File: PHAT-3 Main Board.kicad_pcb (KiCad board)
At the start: 2 copper layers, 18 parts, among them P1 Power Terminal Block, P2 Power Terminal Block, P3 Power Terminal Block, P4 Power Terminal Block, Q1 IRLZ44N, U1 AHT21, U10 Logic Level Converter, U2 ESP32-S3 Dual-core SX1262, U3 BME280, U4 GY-521 MPU-6050, U5 LM2596, U6 GT-7U, U7 SCD41, U8 uCAM-III, U9 SD Card Reader

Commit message: Rewired Everything Again
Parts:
- added R4: 100, Resistor_THT:R_Axial_DIN0207_L6.3mm_D2.5mm_P10.16mm_Horizontal, F.Cu at (104.1, 142.8)
- added R5: 10k, Resistor_THT:R_Axial_DIN0207_L6.3mm_D2.5mm_P10.16mm_Horizontal, F.Cu at (104.1, 146.8)
- added R6: 10k, Resistor_THT:R_Axial_DIN0207_L6.3mm_D2.5mm_P10.16mm_Horizontal, F.Cu at (104.1, 150.9)
- added R7: 10k, Resistor_THT:R_Axial_DIN0207_L6.3mm_D2.5mm_P10.16mm_Horizontal, F.Cu at (104.1, 154.9)
- U3: value BME280 -> GY-68 BMP180; footprint Actual Footprint Library:BME280 -> Actual Footprint Library:GY-68 BMP180
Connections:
- R1 pad 2: Net-(U1-SDA) -> Net-(U10-HV1)
- R2 pad 1: Net-(U1-SCL) -> Net-(U10-HV2)
- U1 pad 1: +5V -> +3V3
- U10 pad 1: Net-(U10-LV1) -> Net-(U1-SCL)
- U10 pad 11: Net-(U1-SCL) -> Net-(U10-HV2)
- U10 pad 12: Net-(U1-SDA) -> Net-(U10-HV1)
- U10 pad 2: Net-(U10-LV2) -> Net-(U1-SDA)
- U10 pad 3: Net-(U10-LV) -> +3V3
- U2 pad 13: Net-(U10-LV2) -> Net-(U1-SCL)
- U2 pad 14: Net-(U10-LV1) -> Net-(U1-SDA)
- U2 pad 16: Net-(U10-LV) -> unconnected-(U2-3V3-Pad16)
- U2 pad 17: unconnected-(U2-3V3-Pad17) -> +3V3
- U2 pad 18: unconnected-(U2-GND-Pad18) -> GND
- U2 pad 28: Net-(Q1-G) -> Net-(U2-HTR)
- U3 pad 1: +5V -> +3V3
- U4 pad 3: Net-(U1-SCL) -> Net-(U10-HV1)
- U4 pad 4: Net-(U1-SDA) -> Net-(U10-HV2)
- U7 pad 1: unconnected-(U7-GND-Pad1) -> GND
- U7 pad 2: +5V -> +3V3

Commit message: Updated Footprint Sizes and SD Card Reader
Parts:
- added C1: 100uF, Capacitor_THT:C_Radial_D5.0mm_H11.0mm_P2.00mm, F.Cu at (155.5, 154.9)
- added C2: 100nF, Capacitor_THT:C_Disc_D3.0mm_W2.0mm_P2.50mm, F.Cu at (149.1, 153.4)
- added C3: 100nF, Capacitor_THT:C_Disc_D3.0mm_W2.0mm_P2.50mm, F.Cu at (149.1, 157.0)
- added REF**: MountingHole_3.2mm_M3, MountingHole:MountingHole_3.2mm_M3, F.Cu at (187.3, 128.3)
- added REF**: MountingHole_3.2mm_M3, MountingHole:MountingHole_3.2mm_M3, F.Cu at (101.6, 50.8)
- added REF**: MountingHole_3.2mm_M3, MountingHole:MountingHole_3.2mm_M3, F.Cu at (187.3, 54.6)
- added REF**: MountingHole_3.2mm_M3, MountingHole:MountingHole_3.2mm_M3, F.Cu at (101.6, 130.8)
- U9: value SD Card Reader -> SDHC; footprint Actual Footprint Library:SD Card Reader -> Actual Footprint Library:SDHC
- moved P1 112.1 mm to (218.4, 114.3)
- moved R1 108.4 mm to (266.7, 77.2)
- moved R2 108.4 mm to (266.7, 81.3)
- moved U3 105.6 mm to (266.2, 52.1)
- moved U5 105.3 mm to (23.2, 120.5)
- moved U4 103.7 mm to (63.5, 132.1)
- moved U10 93.3 mm to (250.2, 141.0)
- moved P2 77.2 mm to (131.5, 162.9)
- moved P3 77.2 mm to (131.5, 174.8)
- moved P4 77.2 mm to (131.5, 186.7)
- moved U9 70.2 mm to (226.3, 45.8)
- moved U2 62.7 mm to (143.5, 69.8)
- moved U6 53.2 mm to (121.9, 73.7), turned to 180 degrees
- moved R3 49.4 mm to (207.0, 81.3)
- moved Q1 48.9 mm to (65.7, 167.6)
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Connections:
- U2 pad 29: Net-(U2-CS) -> Net-(U2-MISO)
- U2 pad 30: Net-(U2-SCK) -> Net-(U2-CLK)
- U2 pad 32: Net-(U2-MISO) -> Net-(U2-CS)
- U9 pad 1: Net-(U2-CS) -> +3V3
- U9 pad 2: Net-(U2-SCK) -> Net-(U2-CS)
- U9 pad 4: Net-(U2-MISO) -> Net-(U2-CLK)
- U9 pad 5: +5V -> Net-(U2-MISO)
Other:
- board outline added: 95.9 x 90.2 mm
- copper layers 2 -> 6

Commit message: Made a Preliminary PCB Layout
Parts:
- added C4: 100uF, Capacitor_THT:C_Radial_D5.0mm_H11.0mm_P2.00mm, F.Cu at (188.6, 63.5)
- U1, U3, U7: moved to B.Cu
- moved U5 162.7 mm to (169.5, 49.5), turned to 180 degrees
- moved R2 138.0 mm to (136.5, 127.0)
- moved R1 137.8 mm to (136.5, 122.6)
- moved U10 135.0 mm to (116.9, 119.4)
- moved R4 134.9 mm to (176.5, 95.2), turned to 180 degrees
- moved R5 132.6 mm to (166.4, 90.8)
- moved U4 123.5 mm to (186.7, 123.2), turned to 180 degrees
- moved Q1 122.5 mm to (168.9, 101.6)
- moved C1 110.5 mm to (118.7, 50.8)
- moved U3 104.6 mm to (178.9, 109.9), turned to 180 degrees
- moved U1 98.3 mm to (141.6, 111.1), turned to -90 degrees
- moved P3 94.2 mm to (184.8, 97.2), turned to 90 degrees
- moved U7 93.7 mm to (119.4, 77.6), turned to 90 degrees
- moved R6 73.1 mm to (99.7, 118.7)
- moved R7 72.1 mm to (99.7, 123.8)
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
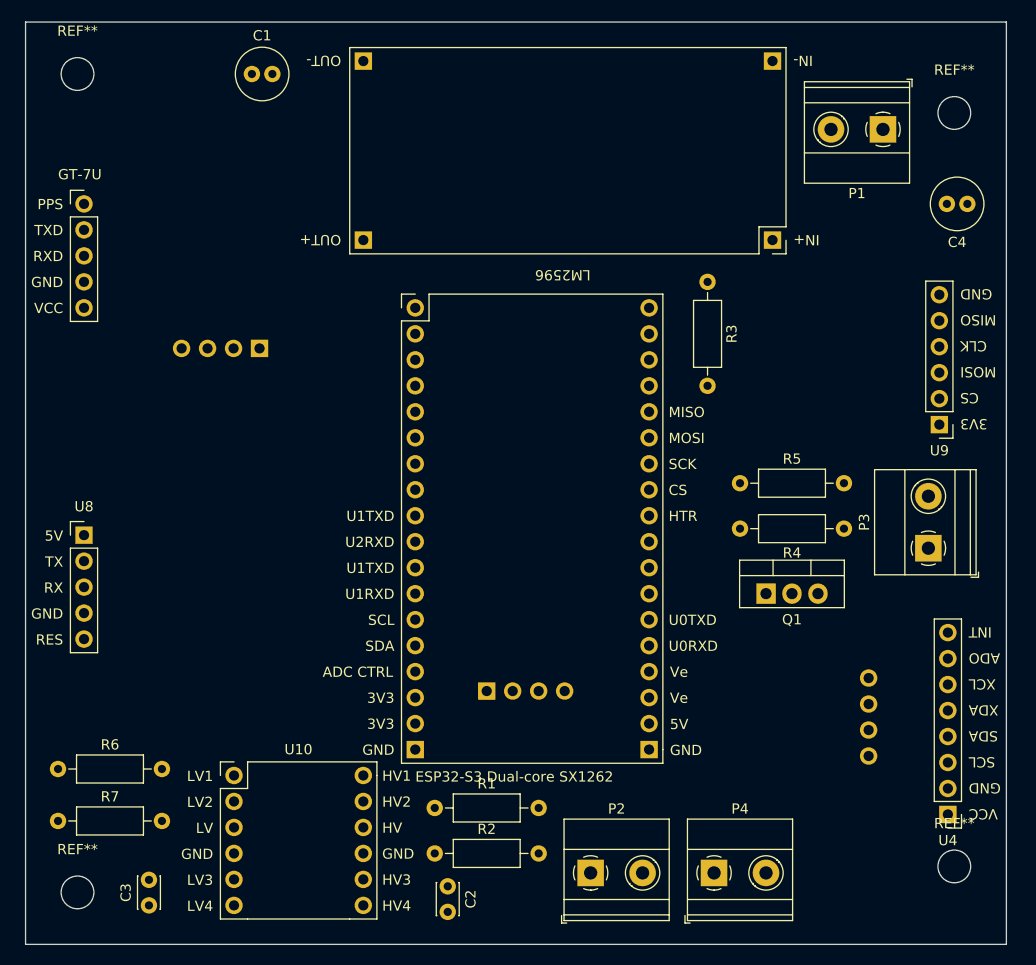
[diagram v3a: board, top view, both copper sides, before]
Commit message: Redid PCB Arrangement
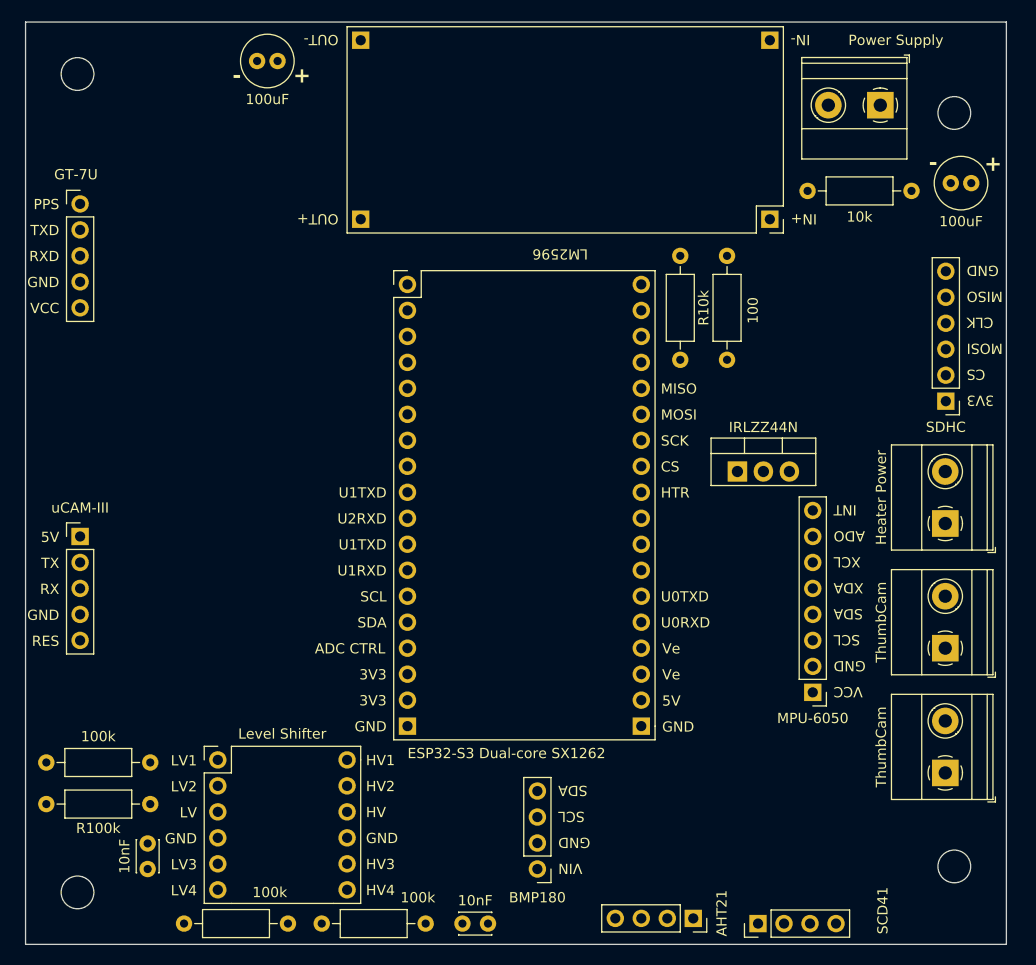
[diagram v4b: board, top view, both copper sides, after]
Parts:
- AHT21: renamed from U1; moved to F.Cu
- BMP180: renamed from U3; moved to F.Cu
- Heater Power: renamed from P3
- Level Shifter: renamed from U10
- Power Supply: renamed from P1
- SCD41: renamed from U7; moved to F.Cu
- moved SCD41 74.4 mm to (168.1, 133.9)
- moved BMP180 37.4 mm to (146.6, 128.5)
- moved ThumbCam 36.0 mm to (186.4, 119.1), turned to 90 degrees
- moved ThumbCam 31.5 mm to (186.4, 106.9), turned to 90 degrees
- moved AHT21 30.0 mm to (161.8, 133.3)
- moved 100k 25.5 mm to (112.0, 133.9)
- moved R10k 23.0 mm to (160.5, 68.6), turned to -90 degrees
- moved 10k 21.8 mm to (183.1, 62.2), turned to 180 degrees
- moved 100 20.1 mm to (165.1, 78.7), turned to 90 degrees
- moved MPU-6050 17.8 mm to (173.5, 111.3)
- moved 100k 15.8 mm to (125.5, 133.9)
- moved IRLZZ44N 12.3 mm to (166.1, 89.7)
- moved 100k 10.7 mm to (108.7, 118.1), turned to 180 degrees
- moved R100k 9.65 mm to (108.7, 122.2), turned to 180 degrees
- moved 10nF 3.92 mm to (139.2, 133.9), turned to 0 degrees
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- renumbered R4 to 100, R2 to 100k, R1 to 100k, R7 to 100k, C4 to 100uF, C1 to 100uF, R3 to 10k, C3 to 10nF, C2 to 10nF, Q1 to IRLZZ44N, U4 to MPU-6050, R6 to R100k, R5 to R10k, U9 to SDHC, P4 to ThumbCam, P2 to ThumbCam, U8 to uCAM-III
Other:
- board text added: "+"
- board text added: "-"

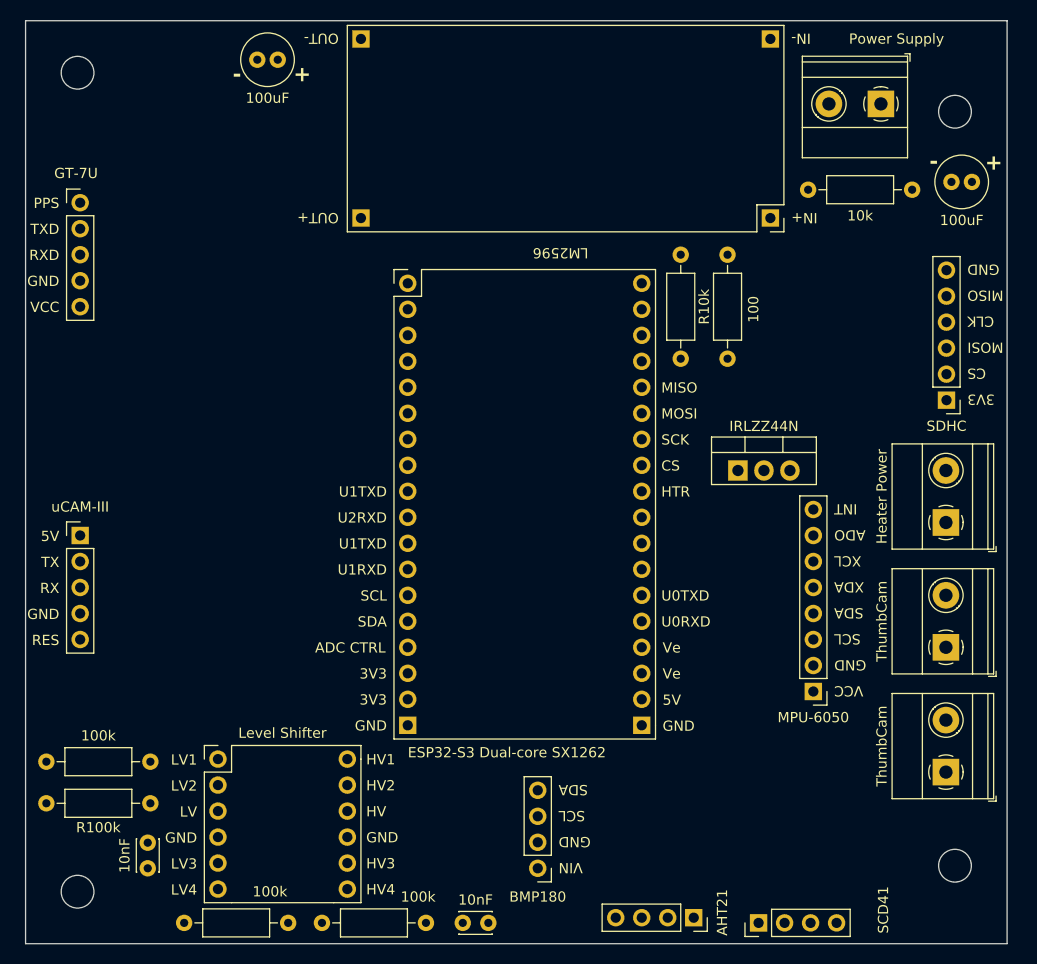
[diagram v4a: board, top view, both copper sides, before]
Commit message: Tweaked Silk Screens and Gave Sensors More Room
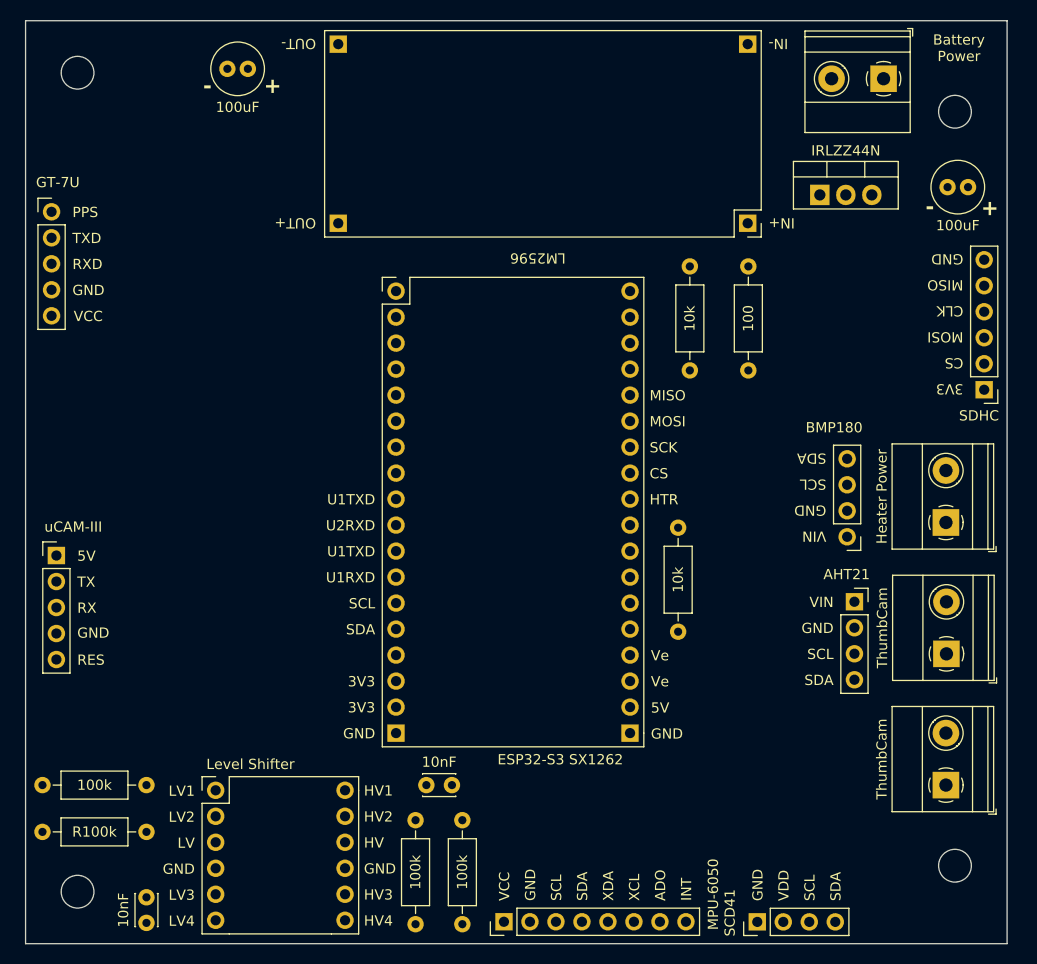
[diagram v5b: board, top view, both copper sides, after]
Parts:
- Battery: renamed from Power Supply
- moved 10k 48.9 mm to (160.3, 105.4), turned to 90 degrees
- moved BMP180 44.3 mm to (176.8, 96.1)
- moved MPU-6050 37.7 mm to (143.3, 133.7), turned to 90 degrees
- moved AHT21 34.6 mm to (177.5, 102.5), turned to 0 degrees
- moved IRLZZ44N 28.1 mm to (174.1, 62.7)
- moved 100k 24.7 mm to (134.6, 123.8), turned to -90 degrees
- moved 100k 17.0 mm to (139.2, 123.8), turned to -90 degrees
- moved 10nF 13.9 mm to (135.7, 120.4)
- moved 10nF 5.34 mm to (108.3, 133.9)
- moved SDHC 3.82 mm to (190.2, 81.8)
- moved Level Shifter 3.06 mm to (115.1, 120.9)
- moved 100uF 3.05 mm to (118.2, 50.4)
- moved uCAM-III 3.04 mm to (99.5, 98.0)
- moved U6 2.93 mm to (99.1, 64.4)
- moved R100k 2.82 mm to (108.3, 125.0)
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- renumbered R10k to 10k
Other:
- board text added: "Battery Power"

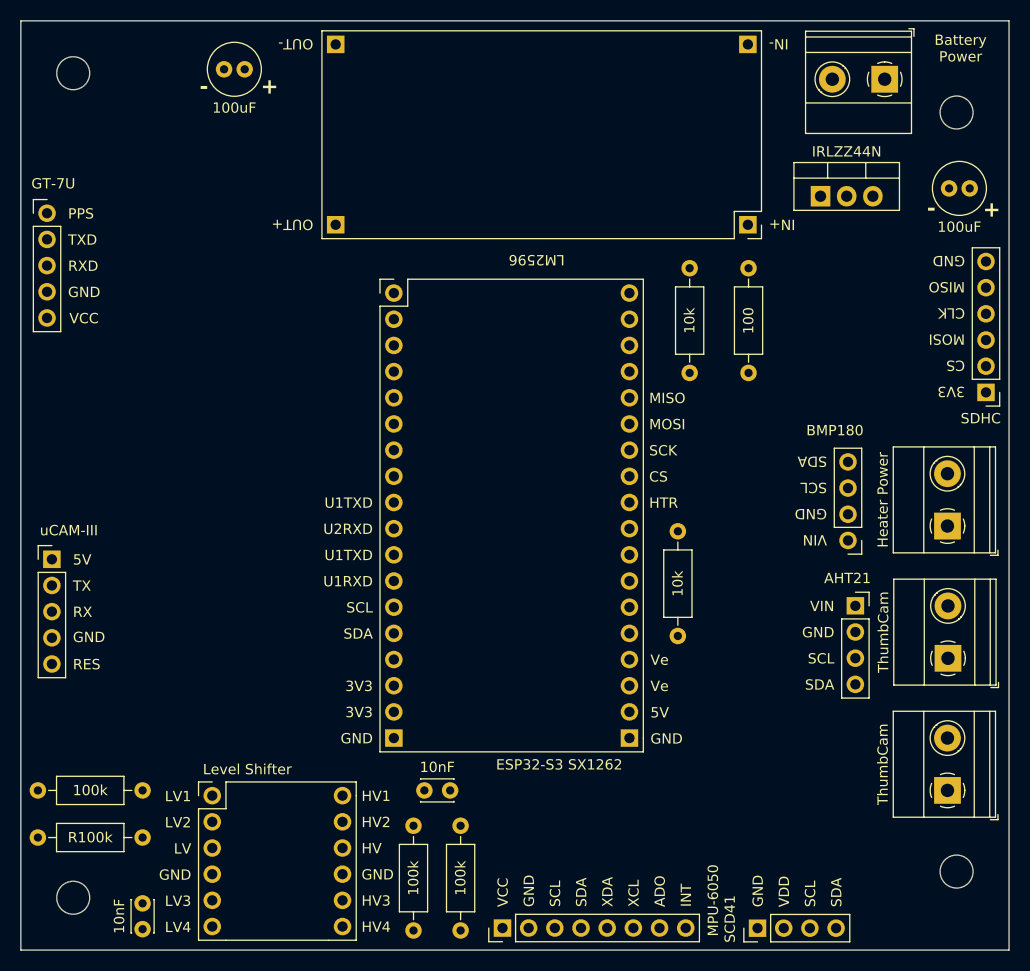
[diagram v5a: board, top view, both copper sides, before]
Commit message: Added Diodes and Switch
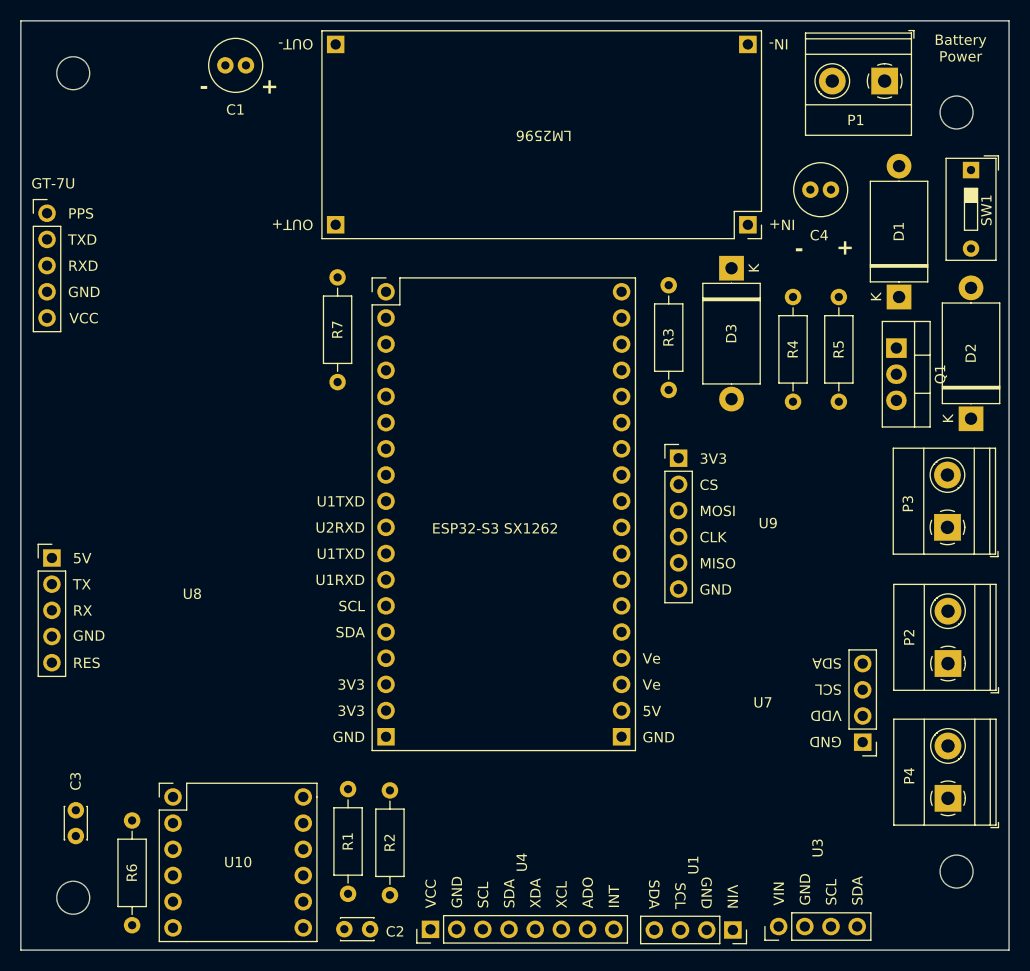
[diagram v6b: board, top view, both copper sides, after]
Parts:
- removed 100: 100, Resistor_THT:R_Axial_DIN0207_L6.3mm_D2.5mm_P10.16mm_Horizontal
- removed 100k (x3), 10k (x2), R100k: 10k, Resistor_THT:R_Axial_DIN0207_L6.3mm_D2.5mm_P10.16mm_Horizontal
- removed 100uF (x2): 100uF, Capacitor_THT:C_Radial_D5.0mm_H11.0mm_P2.00mm
- removed 10nF (x2): 100nF, Capacitor_THT:C_Disc_D3.0mm_W2.0mm_P2.50mm
- removed AHT21: AHT21, Actual Footprint Library:AHT21
- removed BMP180: GY-68 BMP180, Actual Footprint Library:GY-68 BMP180
- removed Battery, ThumbCam (x2): Power Terminal Block, TerminalBlock_Phoenix:TerminalBlock_Phoenix_MKDS-1,5-2-5.08_1x02_P5.08mm_Horizontal
- removed Heater Power: Power Terminal Block, TerminalBlock_Phoenix:TerminalBlock_Phoenix_MKDS-1,5-2-5.08_1x02_P5.08mm_Horizontal
- removed IRLZZ44N: IRLZ44N, Package_TO_SOT_THT:TO-220-3_Vertical
- removed Level Shifter: Logic Level Converter, Actual Footprint Library:Logic Level Converter
- removed MPU-6050: GY-521 MPU-6050, Actual Footprint Library:GY-521 MPU-6050
- removed SCD41: SCD41, Actual Footprint Library:SCD41
- removed SDHC: SDHC, Actual Footprint Library:SDHC
- removed uCAM-III: uCAM-III, Actual Footprint Library:uCAM-III
- added C1: 100uF, Capacitor_THT:C_Radial_D5.0mm_H11.0mm_P2.00mm, F.Cu at (116.4, 50.0)
- added C2: 100nF, Capacitor_THT:C_Disc_D3.0mm_W2.0mm_P2.50mm, F.Cu at (127.9, 133.9)
- added C3: 100nF, Capacitor_THT:C_Disc_D3.0mm_W2.0mm_P2.50mm, F.Cu at (101.9, 122.3)
- added C4: 100uF, Capacitor_THT:C_Radial_D5.0mm_H11.0mm_P2.00mm, F.Cu at (173.1, 62.1)
- added D1: ~, Diode_THT:D_DO-27_P12.70mm_Horizontal, F.Cu at (181.7, 72.5)
- added D2: ~, Diode_THT:D_DO-27_P12.70mm_Horizontal, F.Cu at (188.7, 84.3)
- added D3: ~, Diode_THT:D_DO-27_P12.70mm_Horizontal, F.Cu at (165.5, 69.7)
- added P1: Power Terminal Block, TerminalBlock_Phoenix:TerminalBlock_Phoenix_MKDS-1,5-2-5.08_1x02_P5.08mm_Horizontal, F.Cu at (180.3, 51.6)
- added P2: Power Terminal Block, TerminalBlock_Phoenix:TerminalBlock_Phoenix_MKDS-1,5-2-5.08_1x02_P5.08mm_Horizontal, F.Cu at (186.5, 108.1)
- added P3: Power Terminal Block, TerminalBlock_Phoenix:TerminalBlock_Phoenix_MKDS-1,5-2-5.08_1x02_P5.08mm_Horizontal, F.Cu at (186.4, 94.9)
- added P4: Power Terminal Block, TerminalBlock_Phoenix:TerminalBlock_Phoenix_MKDS-1,5-2-5.08_1x02_P5.08mm_Horizontal, F.Cu at (186.5, 121.2)
- added Q1: IRLZ44N, Package_TO_SOT_THT:TO-220-3_Vertical, F.Cu at (181.5, 77.5)
- added R1: 10k, Resistor_THT:R_Axial_DIN0207_L6.3mm_D2.5mm_P10.16mm_Horizontal, F.Cu at (128.3, 130.4)
- added R2: 10k, Resistor_THT:R_Axial_DIN0207_L6.3mm_D2.5mm_P10.16mm_Horizontal, F.Cu at (132.3, 130.6)
- added R3: 10k, Resistor_THT:R_Axial_DIN0207_L6.3mm_D2.5mm_P10.16mm_Horizontal, F.Cu at (159.4, 81.5)
- added R4: 100, Resistor_THT:R_Axial_DIN0207_L6.3mm_D2.5mm_P10.16mm_Horizontal, F.Cu at (171.4, 72.5)
- added R5: 10k, Resistor_THT:R_Axial_DIN0207_L6.3mm_D2.5mm_P10.16mm_Horizontal, F.Cu at (175.9, 72.5)
- added R6: 10k, Resistor_THT:R_Axial_DIN0207_L6.3mm_D2.5mm_P10.16mm_Horizontal, F.Cu at (107.3, 123.3)
- added R7: 10k, Resistor_THT:R_Axial_DIN0207_L6.3mm_D2.5mm_P10.16mm_Horizontal, F.Cu at (127.3, 70.6)
- added SW1: SW_Push_SPDT, Button_Switch_THT:SW_DIP_SPSTx01_Slide_9.78x4.72mm_W7.62mm_P2.54mm, F.Cu at (188.7, 60.2)
- added U1: AHT21, Actual Footprint Library:AHT21, F.Cu at (165.6, 133.9)
- added U10: Logic Level Converter, Actual Footprint Library:Logic Level Converter, F.Cu at (111.3, 121.0)
- added U3: GY-68 BMP180, Actual Footprint Library:GY-68 BMP180, F.Cu at (170.1, 133.6)
- added U4: GY-521 MPU-6050, Actual Footprint Library:GY-521 MPU-6050, F.Cu at (136.3, 133.9)
- added U7: SCD41, Actual Footprint Library:SCD41, F.Cu at (178.2, 115.7)
- added U8: uCAM-III, Actual Footprint Library:uCAM-III, F.Cu at (99.5, 97.8)
- added U9: SDHC, Actual Footprint Library:SDHC, F.Cu at (160.3, 88.2)
- moved U2 0.77 mm to (132.0, 72.0)
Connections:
- U5 pad 3: GND -> Net-(D1-A)
